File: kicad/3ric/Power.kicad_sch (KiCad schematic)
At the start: 49 parts

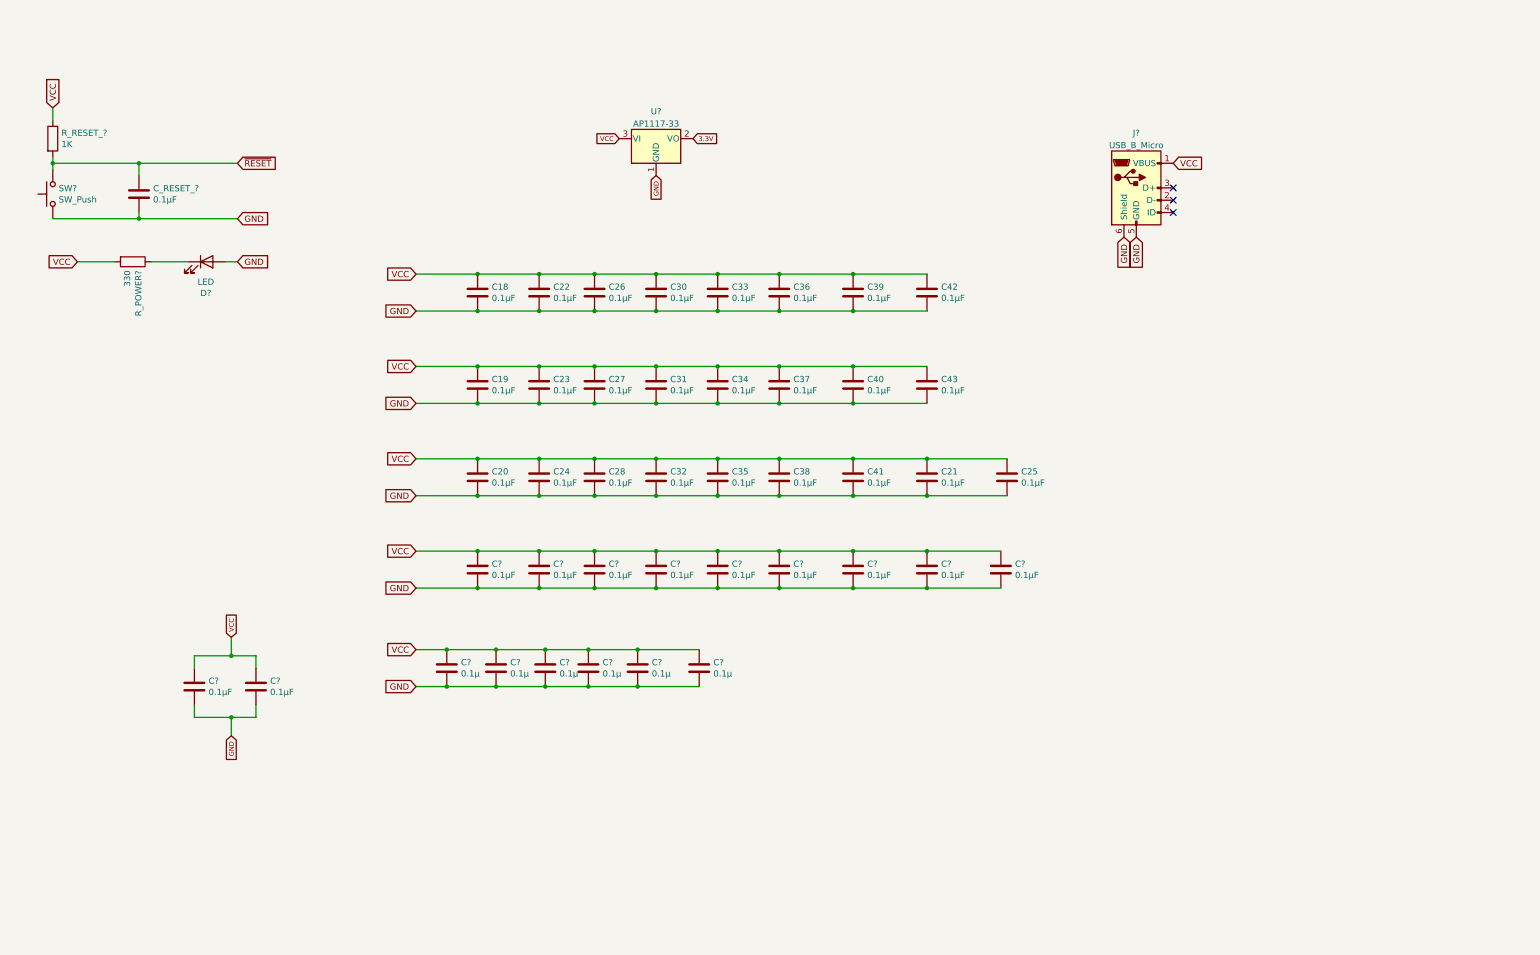
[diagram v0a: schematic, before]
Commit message: stash latest simulation and schematic changes - adding untested soft switches and RAM banking
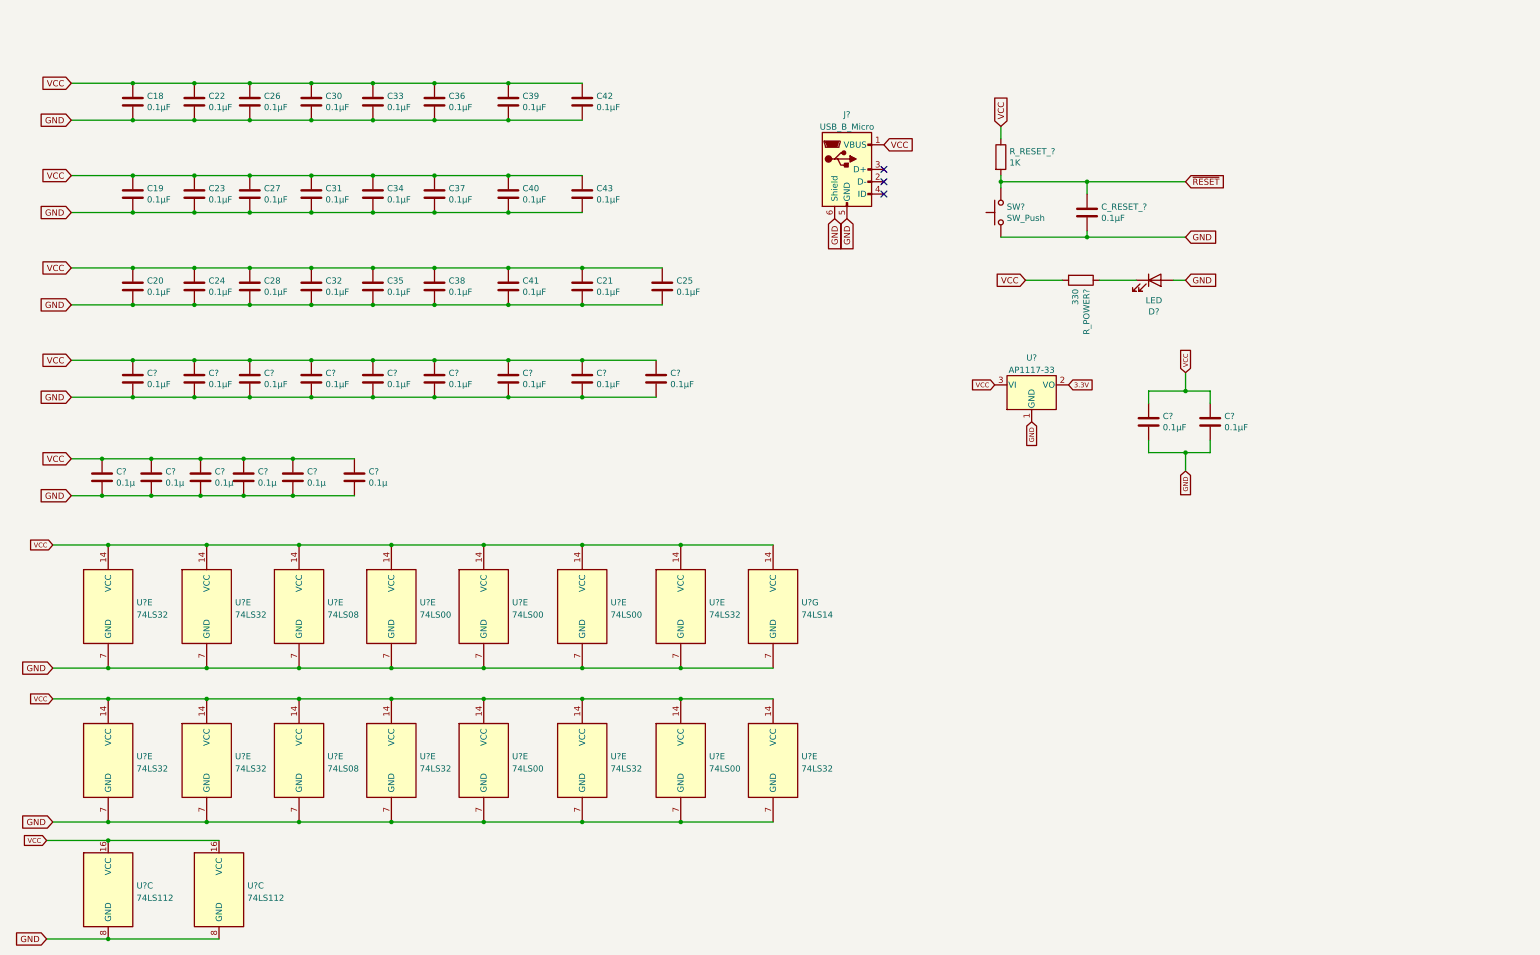
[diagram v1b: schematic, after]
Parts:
- added U? (x8): 74LS32, symbol 74xx:74LS32
- added U? (x5): 74LS00, symbol 74xx:74LS00
- added U? (x2): 74LS08, symbol 74xx:74LS08
- added U?: 74LS14, symbol 74xx:74LS14
- added U? (x2): 74LS112, symbol 74xx:74LS112
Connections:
- net GND: now also U?.7 (GND), U?.7 (GND), U?.7 (GND), U?.7 (GND), U?.7 (GND), U?.7 (GND), U?.7 (GND), U?.7 (GND), U?.7 (GND), U?.7 (GND), U?.7 (GND), U?.7 (GND), U?.7 (GND), U?.7 (GND), U?.7 (GND), U?.7 (GND), U?.8 (GND), U?.8 (GND)
- net VCC: now also U?.14 (VCC), U?.14 (VCC), U?.14 (VCC), U?.14 (VCC), U?.14 (VCC), U?.14 (VCC), U?.14 (VCC), U?.14 (VCC), U?.14 (VCC), U?.14 (VCC), U?.14 (VCC), U?.14 (VCC), U?.14 (VCC), U?.14 (VCC), U?.14 (VCC), U?.14 (VCC), U?.16 (VCC), U?.16 (VCC)
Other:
- moved on the sheet: C18, C19, C20, C21, C22, C23, C24, C25, C26, C27, C28, C30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

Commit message: push schematic updates
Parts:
- added U? (x7): 74LS08, symbol 74xx:74LS08
- added U? (x5): 74LS00, symbol 74xx:74LS00
- added U? (x5): 74LS04, symbol 74xx:74LS04
- added U? (x2): 74LS32, symbol 74xx:74LS32
- added U_NOT_DECODE?: 74LS14, Package_DIP:DIP-14_W7.62mm_Socket, symbol 74xx:74LS14
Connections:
- net GND: now also U?.7 (GND), U?.7 (GND), U?.7 (GND), U?.7 (GND), U?.7 (GND), U?.7 (GND), U?.7 (GND), U?.7 (GND), U?.7 (GND), U?.7 (GND), U_NOT_DECODE?.7 (GND)
- net VCC: now also U?.14 (VCC), U?.14 (VCC), U?.14 (VCC), U?.14 (VCC), U?.14 (VCC), U?.14 (VCC), U?.14 (VCC), U?.14 (VCC), U?.14 (VCC), U?.14 (VCC), U_NOT_DECODE?.14 (VCC)
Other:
- moved on the sheet: C19, C20, C21, C23, C24, C25, C27, C28, C31, C32, C34, C35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

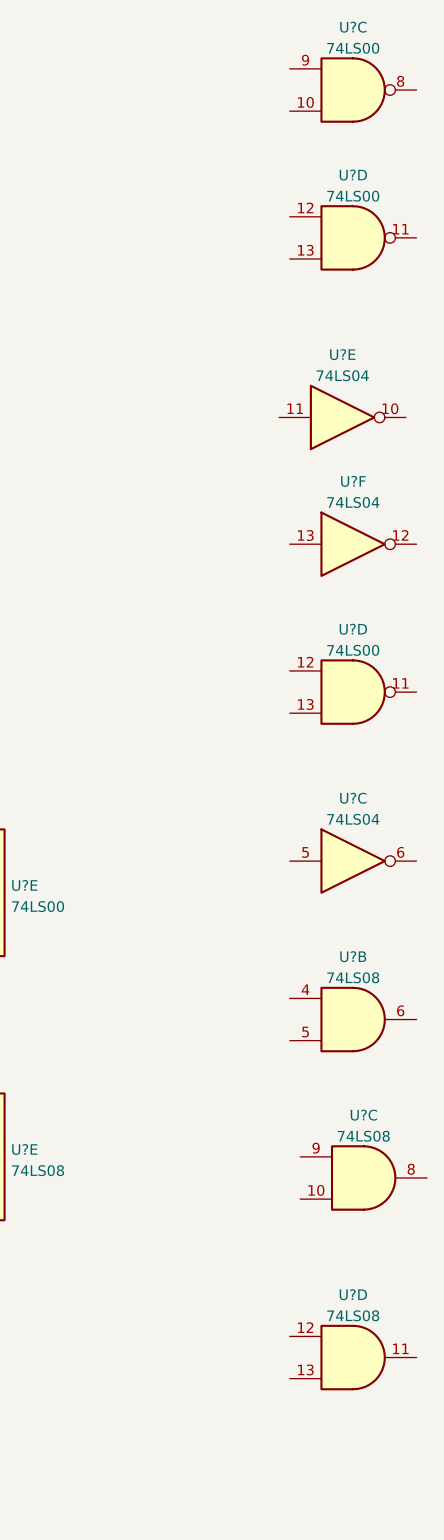
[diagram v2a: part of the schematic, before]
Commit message: upgraded to kicad 8, updates to schematic - added snes controllers, mouse port, many fixes
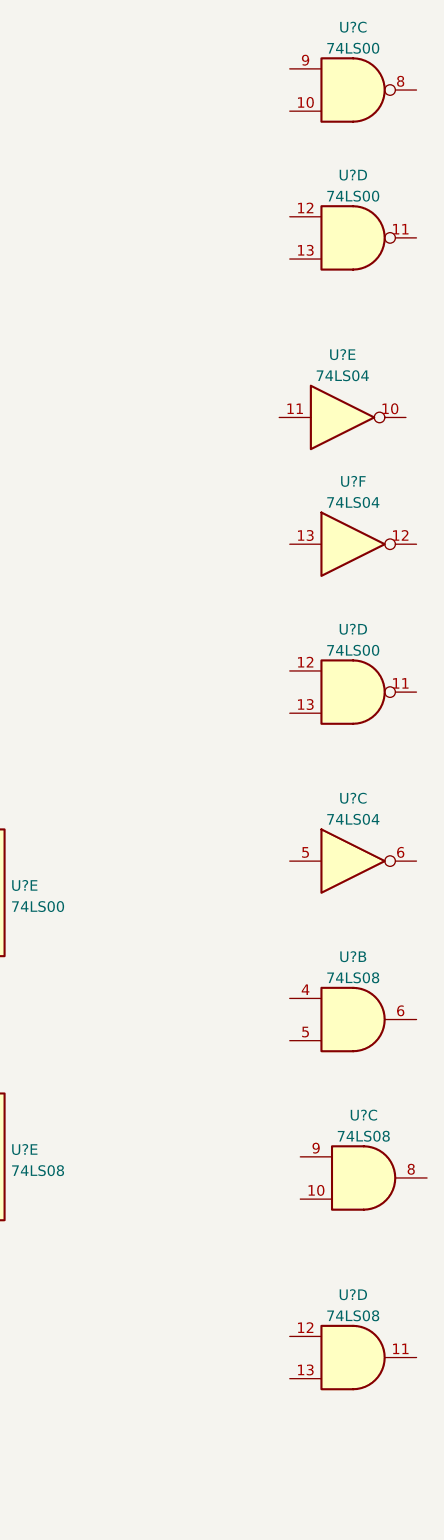
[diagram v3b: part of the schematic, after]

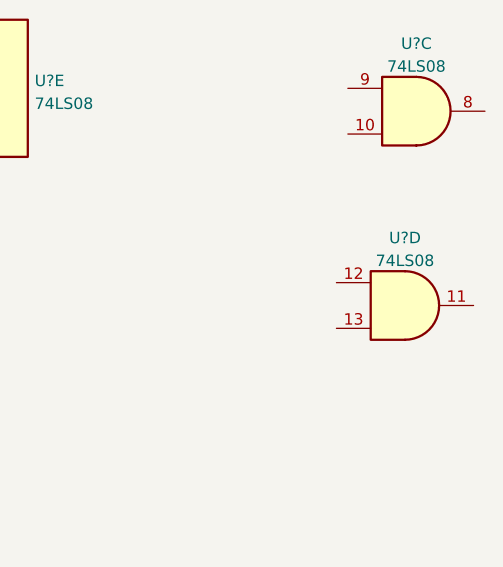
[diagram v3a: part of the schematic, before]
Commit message: update schematic to include disk components
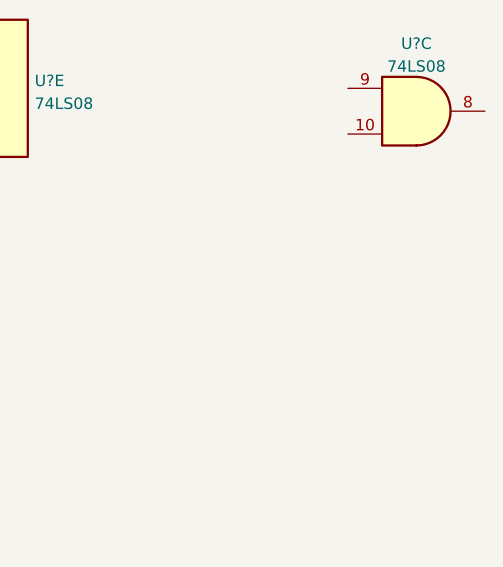
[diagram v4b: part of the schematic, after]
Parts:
- removed U?: 74LS08, symbol 74xx:74LS08
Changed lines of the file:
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@@
-	)
-	(symbol
-		(lib_id "74xx:74LS08")
-		(at 317.5 165.1 0)
-		(unit 4)
-		(exclude_from_sim no)
-		(in_bom yes)
-		(on_board yes)
-		(dnp no)
-		(fields_autoplaced yes)
-		(property "Reference" "U?"
-			(at 317.5 157.5902 0)
-			(effects
-				(font
-					(size 1.27 1.27)
-				)
-			)
-		)
-		(property "Value" "74LS08"
-			(at 317.5 160.1271 0)
-			(effects
-				(font
-					(size 1.27 1.27)
-				)
-			)
-		)
-		(property "Footprint" ""
-			(at 317.5 165.1 0)
-			(effects
-				(font
-					(size 1.27 1.27)
-				)
-				(hide yes)
-			)
-		)
-		(property "Datasheet" "http://www.ti.com/lit/gpn/sn74LS08"
-			(at 317.5 165.1 0)
-			(effects
-				(font
-					(size 1.27 1.27)
-				)
-				(hide yes)
-			)
-		)
-		(property "Description" ""
-			(at 317.5 165.1 0)
-			(effects
-				(font
-					(size 1.27 1.27)
-				)
-				(hide yes)
-			)
-		)
-		(pin "1"
-		)
-		(pin "2"
-		)
-		(pin "3"
-		)
-		(pin "4"
-		)
-		(pin "5"
-		)
-		(pin "6"
-		)
-		(pin "10"
-		)
-		(pin "8"
-		)
-		(pin "9"
-		)
-		(pin "11"
-		)
-		(pin "12"
-		)
-		(pin "13"
-		)
-		(pin "14"
-		)
-		(pin "7"
-		)
-		(instances
-			(project "3ric"
-				(path "/e63e39d7-6ac0-4ffd-8aa3-1841a4541b55/764b565a-6190-4617-a6c7-5dd4a5c3617c"
-					(reference "U?")
-					(unit 4)
-				)
-			)
-		)
 	)
 	(symbol

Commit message: cleaning up of the schematic
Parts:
- removed U? (x4): 74LS08, symbol 74xx:74LS08
- removed U? (x5): 74LS00, symbol 74xx:74LS00
- removed U? (x4): 74LS04, symbol 74xx:74LS04
- removed U?: 74LS112, symbol 74xx:74LS112
- removed U?: 74LS32, symbol 74xx:74LS32
- removed U_NOT_DECODE?: 74LS14, Package_DIP:DIP-14_W7.62mm_Socket, symbol 74xx:74LS14
- added F4: 74LS112, Package_DIP:DIP-16_W7.62mm_Socket, symbol 74xx:74LS112
- A1, A2, A4, A5, B2, B4, B5, B6, B7, C1, D2, D3, D4, E1, E6, F1, F2, F5, W1, W7: renamed from U?; footprint (none) -> Package_DIP:DIP-14_W7.62mm_Socket
- F3: renamed from U?; footprint (none) -> Package_DIP:DIP-16_W7.62mm_Socket
- gave numbers to parts that had none: 24
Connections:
- net GND: now also F4.8 (GND)
- net VCC: now also F4.16 (VCC)

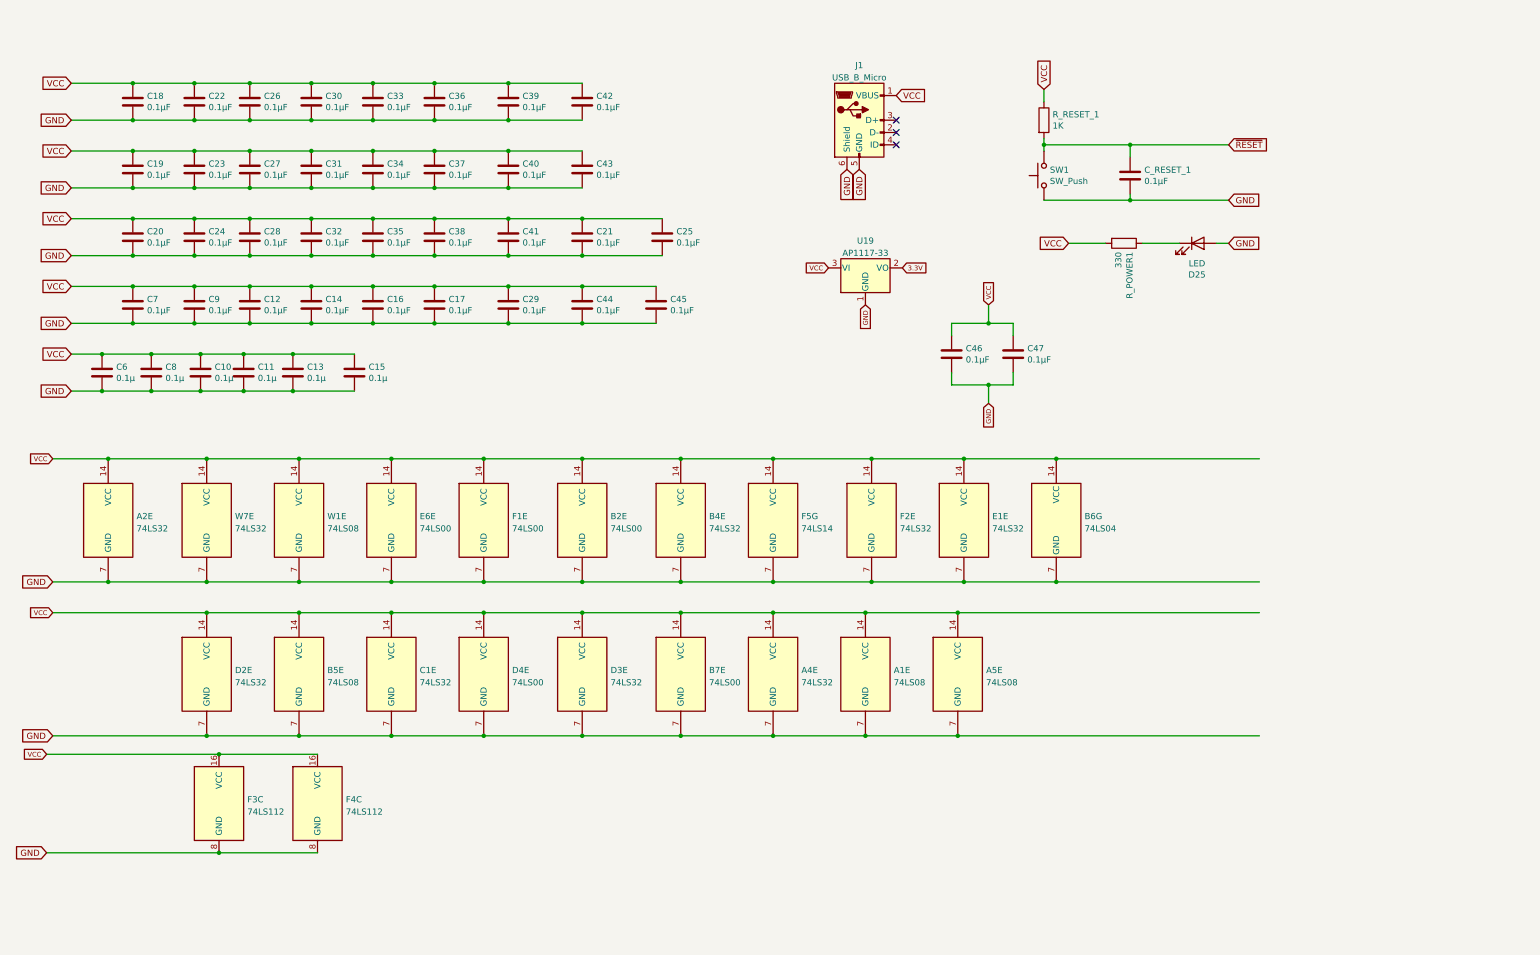
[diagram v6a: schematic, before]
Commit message: updated schematics and PCB PNG of the breadboard layout
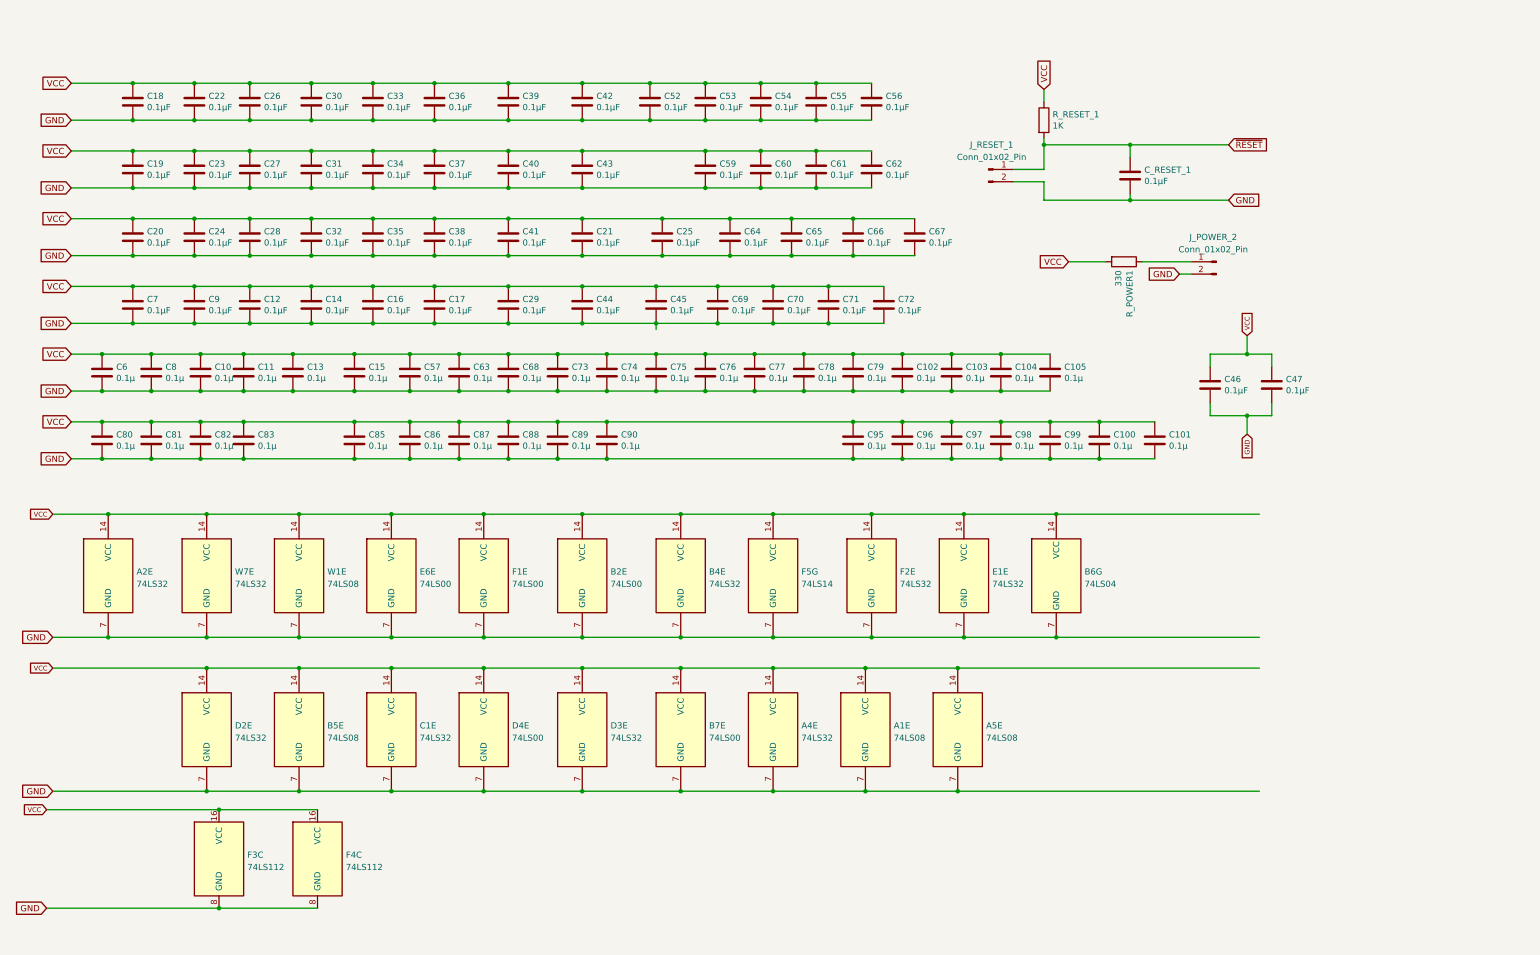
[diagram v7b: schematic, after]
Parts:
- removed D25: LED, LED_THT:LED_D5.0mm, symbol Device:LED
- removed J1: USB_B_Micro, Connector_USB:USB_Micro-B_Molex-105017-0001, symbol Connector:USB_B_Micro
- removed SW1: SW_Push, Button_Switch_THT:SW_PUSH_6mm, symbol Switch:SW_Push
- removed U19: AP1117-33, Package_TO_SOT_SMD:SOT-223-3_TabPin2, symbol Regulator_Linear:AP1117-33
- added C100, C101, C102, C103, C104, C105, C57, C63, C68, C73, C74, C75, C76, C77, C78, C79, C80, C81, C82, C83, C85, C86, C87, C88, C89, C90, C95, C96, C97, C98, C99: 0.1µ, Capacitor_SMD:C_1206_3216Metric_Pad1.33x1.80mm_HandSolder, symbol Device:C
- added C52, C53, C54, C55, C56, C59, C60, C61, C62, C64, C65, C66, C67, C69, C70, C71, C72: 0.1µF, Capacitor_SMD:C_1206_3216Metric_Pad1.33x1.80mm_HandSolder, symbol Device:C
- added J_POWER_2, J_RESET_1: Conn_01x02_Pin, Connector_PinHeader_2.54mm:PinHeader_2x01_P2.54mm_Vertical, symbol Connector:Conn_01x02_Pin
- C10, C11, C12, C13, C14, C15, C16, C17, C18, C19, C20, C21, C22, C23, C24, C25, C26, C27, C28, C29, C30, C31, C32, C33, C34, C35, C36, C37, C38, C39, C40, C41, C42, C43, C44, C45, C46, C47, C6, C7, C8, C9, C_RESET_1: footprint Capacitor_THT:C_Axial_L3.8mm_D2.6mm_P7.50mm_Horizontal -> Capacitor_SMD:C_1206_3216Metric_Pad1.33x1.80mm_HandSolder
- R_POWER1: footprint Resistor_THT:R_Axial_DIN0207_L6.3mm_D2.5mm_P7.62mm_Horizontal -> Resistor_SMD:R_0603_1608Metric_Pad0.98x0.95mm_HandSolder
- R_RESET_1: footprint Resistor_THT:R_Axial_DIN0207_L6.3mm_D2.5mm_P7.62mm_Horizontal -> Resistor_SMD:R_0805_2012Metric_Pad1.20x1.40mm_HandSolder
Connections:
- net GND: now also C100.2, C101.2, C102.2, C103.2, C104.2, C105.2, C52.2, C53.2, C54.2, C55.2, C56.2, C57.2, C59.2, C60.2, C61.2, C62.2, C63.2, C64.2, C65.2, C66.2, C67.2, C68.2, C69.2, C70.2, C71.2, C72.2, C73.2, C74.2, C75.2, C76.2, C77.2, C78.2, C79.2, C80.2, C81.2, C82.2, C83.2, C85.2, C86.2, C87.2, C88.2, C89.2, C90.2, C95.2, C96.2, C97.2, C98.2, C99.2, J_POWER_2.2 (Pin_2), J_RESET_1.2 (Pin_2)
- net VCC: now also C100.1, C101.1, C102.1, C103.1, C104.1, C105.1, C52.1, C53.1, C54.1, C55.1, C56.1, C57.1, C59.1, C60.1, C61.1, C62.1, C63.1, C64.1, C65.1, C66.1, C67.1, C68.1, C69.1, C70.1, C71.1, C72.1, C73.1, C74.1, C75.1, C76.1, C77.1, C78.1, C79.1, C80.1, C81.1, C82.1, C83.1, C85.1, C86.1, C87.1, C88.1, C89.1, C90.1, C95.1, C96.1, C97.1, C98.1, C99.1
- net ~{RESET}: now also J_RESET_1.1 (Pin_1)
- net at R_POWER1.1: now also J_POWER_2.1 (Pin_1)
- no-connect marks 3 -> 0
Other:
- moved on the sheet: A1E, A2E, A4E, A5E, B2E, B4E, B5E, B6G, B7E, C1E, C46, C47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

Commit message: pcb layout continued
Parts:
- removed J_POWER_2: Conn_01x02_Pin, Connector_PinHeader_2.54mm:PinHeader_2x01_P2.54mm_Vertical, symbol Connector:Conn_01x02_Pin
- removed R_POWER1: 330, Resistor_SMD:R_0603_1608Metric_Pad0.98x0.95mm_HandSolder, symbol Device:R
